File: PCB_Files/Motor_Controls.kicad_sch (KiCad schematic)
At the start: 10 parts, among them U1 TB6612FNG, U3 TB6612FNG

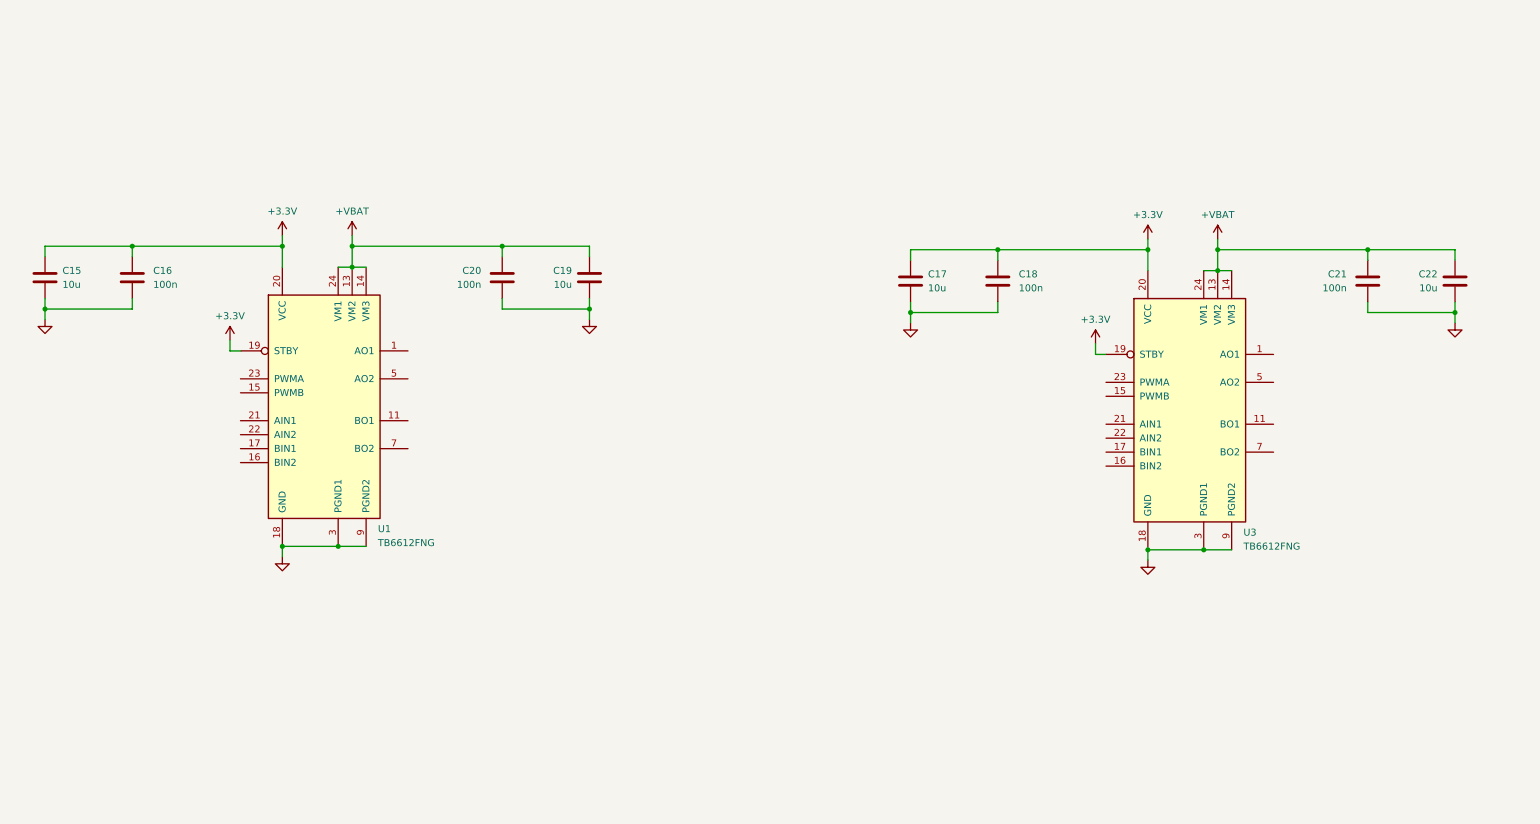
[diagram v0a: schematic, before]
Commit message: Began laying out power schematic and motor controller schematic
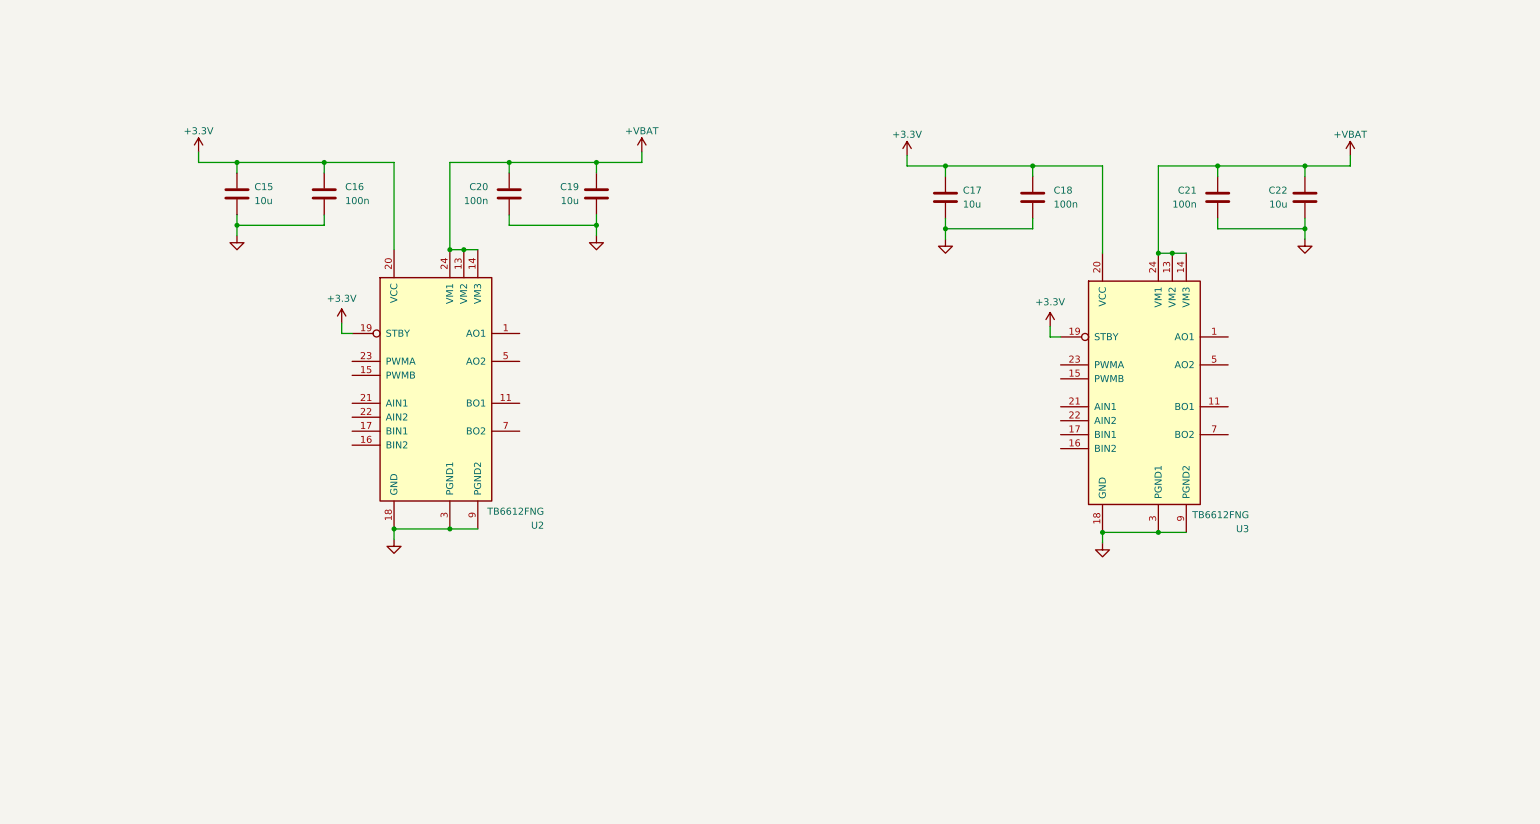
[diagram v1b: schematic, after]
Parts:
- renumbered U1 to U2
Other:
- moved on the sheet: C15, C16, C19, C20, U2

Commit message: Completed motor control schematic sheet and related MCU pin outs.
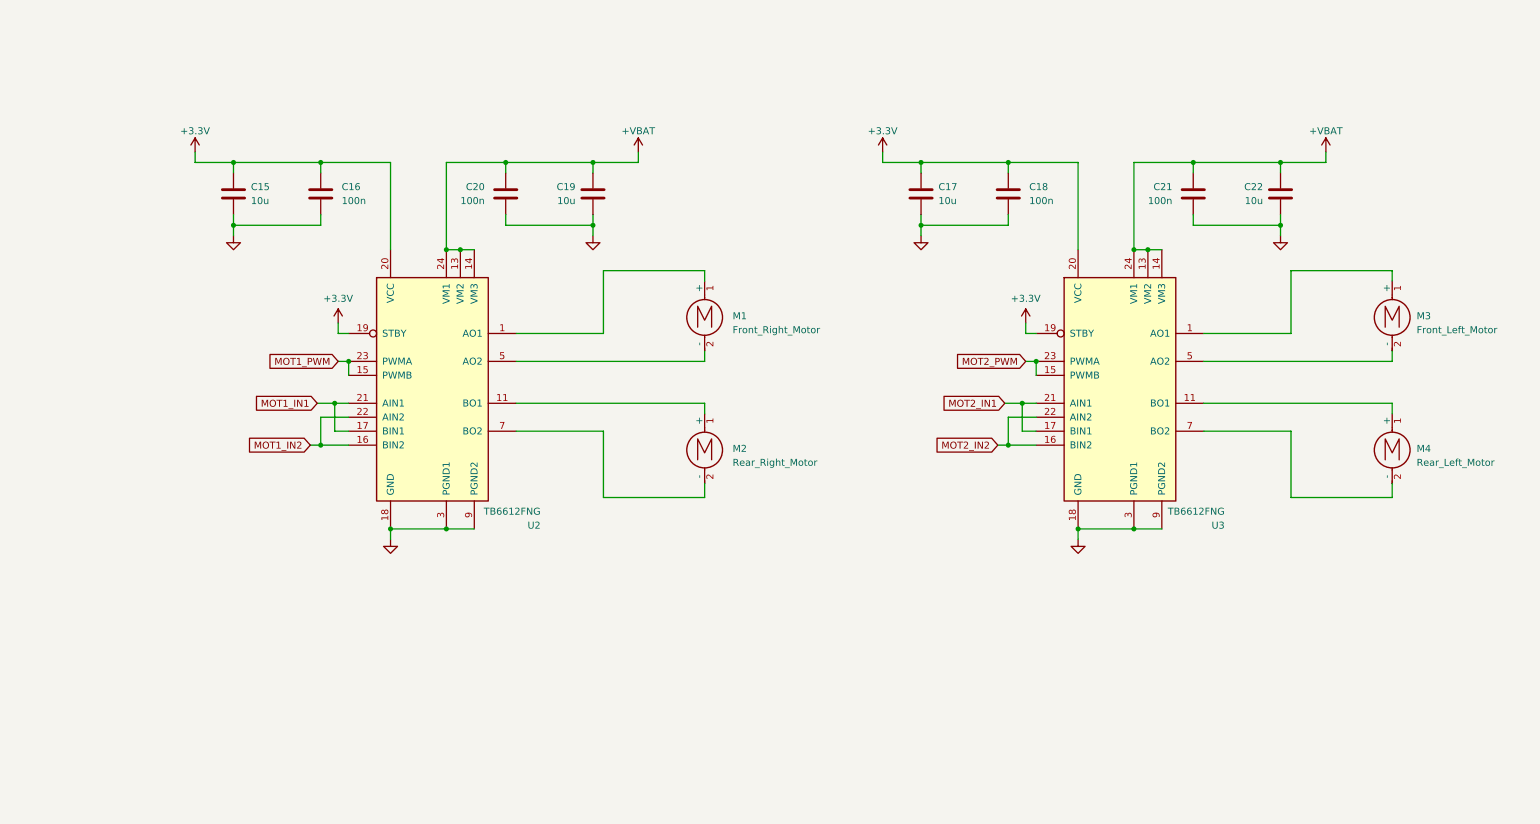
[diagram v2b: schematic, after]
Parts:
- added M1: Front_Right_Motor, symbol Motor:Motor_DC
- added M2: Rear_Right_Motor, symbol Motor:Motor_DC
- added M3: Front_Left_Motor, symbol Motor:Motor_DC
- added M4: Rear_Left_Motor, symbol Motor:Motor_DC
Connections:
- net at U3.1 (AO1), U3.2 (AO1): now also M3.1 (+)
- net at U3.11 (BO1), U3.12 (BO1): now also M4.1 (+)
- net MOT2_PWM: now reaches U3.15 (PWMB)
- net MOT2_PWM: now also U3.23 (PWMA)
- net MOT2_IN2: now reaches U3.16 (BIN2)
- net MOT2_IN2: now also U3.22 (AIN2)
- net MOT2_IN1: now reaches U3.17 (BIN1)
- net MOT2_IN1: now also U3.21 (AIN1)
- net at U3.5 (AO2), U3.6 (AO2): now also M3.2 (-)
- net at U3.7 (BO2), U3.8 (BO2): now also M4.2 (-)
- net at U2.1 (AO1), U2.2 (AO1): now also M1.1 (+)
- net at U2.11 (BO1), U2.12 (BO1): now also M2.1 (+)
- net MOT1_PWM: now reaches U2.15 (PWMB)
- net MOT1_PWM: now also U2.23 (PWMA)
- net MOT1_IN2: now reaches U2.16 (BIN2)
- net MOT1_IN2: now also U2.22 (AIN2)
- net MOT1_IN1: now reaches U2.17 (BIN1)
- net MOT1_IN1: now also U2.21 (AIN1)
- net at U2.5 (AO2), U2.6 (AO2): now also M1.2 (-)
- net at U2.7 (BO2), U2.8 (BO2): now also M2.2 (-)
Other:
- moved on the sheet: C15, C16, C17, C18, C19, C20, C21, C22, U2, U3

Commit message: Cleaned up all ERC errors and warnings due to missing Power Flags or misaligned grid.
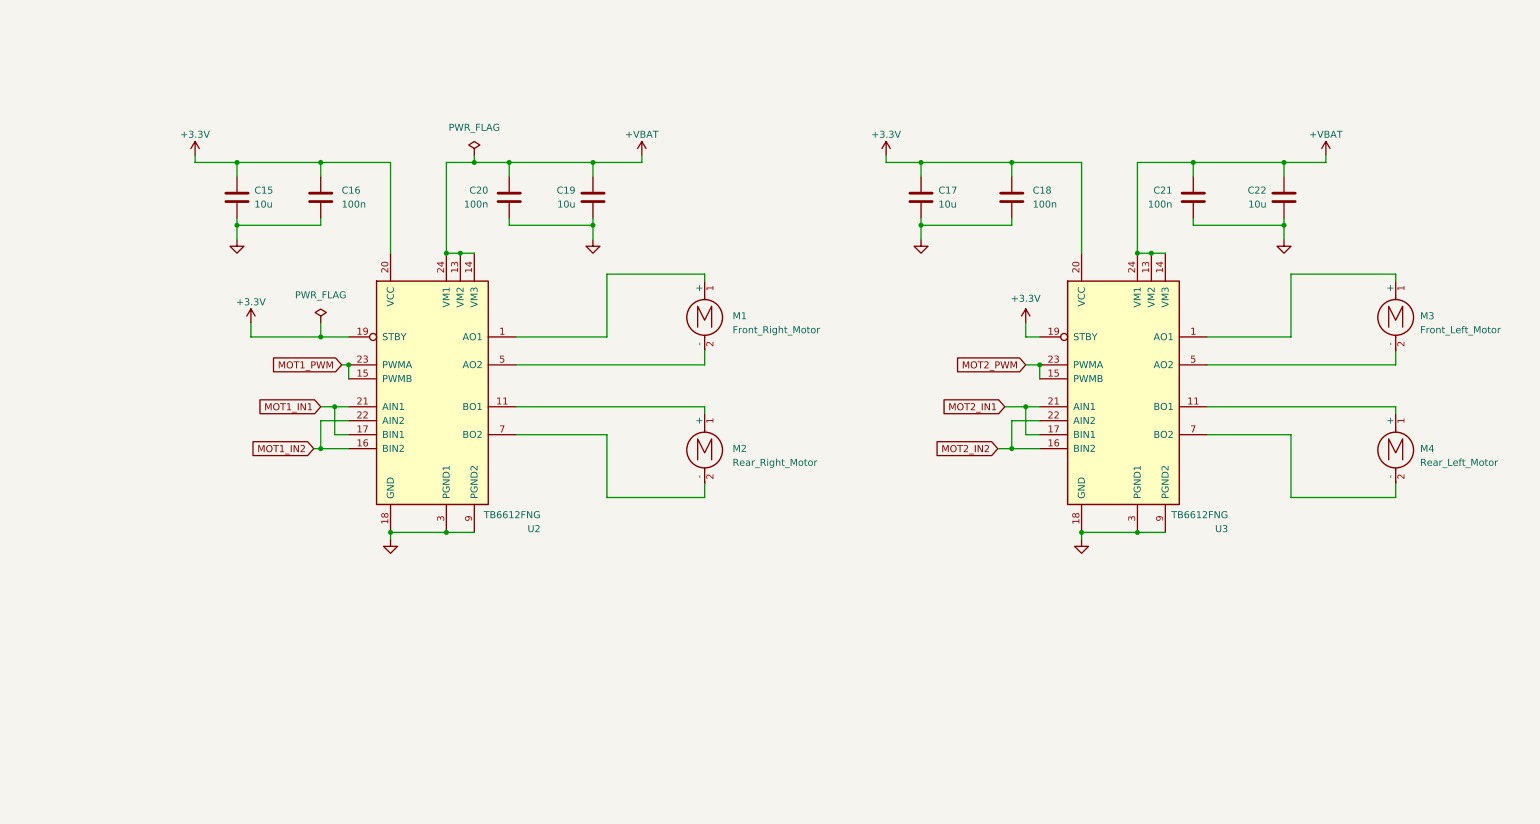
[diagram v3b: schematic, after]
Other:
- moved on the sheet: C15, C16, C17, C18, C19, C20, C21, C22, M3, M4, U2, U3

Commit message: General schematic clean up and footprint allocation.
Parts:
- C15, C16, C17, C18, C19, C20, C21, C22: footprint (none) -> Capacitor_SMD:C_0603_1608Metric
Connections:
- net +3.3V renamed +3V3
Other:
- note added: "MOTOR CONTROLLER - LEFT WHEELS"
- note added: "MOTOR CONTROLLER - RIGHT WHEELS"
- moved on the sheet: C15, C16, C17, C18, C19, C20, C21, C22, M1, M2, M3, M4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

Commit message: Added RadioMaster 2S Battery information to power schematic sheet.
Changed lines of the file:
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@@
-	)
-	(junction
-		(at 179.07 85.09)
-		(diameter 0)
-		(color 0 0 0 0)
 	)
 	(junction
@@
 	(wire
 		(pts
-			(xy 179.07 85.09) (xy 184.15 85.09)
+			(xy 166.37 85.09) (xy 184.15 85.09)
 		)
 		(stroke
@@
 	(wire
 		(pts
-			(xy 179.07 82.55) (xy 179.07 85.09)
-		)
-		(stroke
-			(width 0)
-			(type default)
-		)
-	)
-	(wire
-		(pts
 			(xy 29.21 64.77) (xy 45.72 64.77)
 		)
@@
 		(pts
 			(xy 102.87 52.07) (xy 102.87 53.34)
-		)
-		(stroke
-			(width 0)
-			(type default)
-		)
-	)
-	(wire
-		(pts
-			(xy 166.37 85.09) (xy 179.07 85.09)
 		)
 		(stroke
@@
 					(unit 1)
 				)
-			)
-		)
-	)
-	(symbol
-		(lib_id "power:PWR_FLAG")
-		(at 179.07 82.55 0)
-		(unit 1)
-		(body_style 1)
-		(exclude_from_sim no)
-		(in_bom yes)
-		(on_board yes)
-		(in_pos_files yes)
-		(dnp no)
-		(fields_autoplaced yes)
-		(property "Reference" "#FLG07"
-			(at 179.07 80.645 0)
-			(hide yes)
-			(show_name no)
-			(do_not_autoplace no)
-			(effects
-				(font
-					(size 1.27 1.27)
-				)
-			)
-		)
-		(property "Value" "PWR_FLAG"
-			(at 179.07 77.47 0)
-			(show_name no)
-			(do_not_autoplace no)
-			(effects
-				(font
-					(size 1.27 1.27)
-				)
-			)
-		)
-		(property "Footprint" ""
-			(at 179.07 82.55 0)
-			(hide yes)
-			(show_name no)
-			(do_not_autoplace no)
-			(effects
-				(font
-					(size 1.27 1.27)
-				)
-			)
-		)
-		(property "Datasheet" ""
-			(at 179.07 82.55 0)
-			(hide yes)
-			(show_name no)
-			(do_not_autoplace no)
-			(effects
-				(font
-					(size 1.27 1.27)
-				)
-			)
-		)
-		(property "Description" "Special symbol for telling ERC where power comes from"
-			(at 179.07 82.55 0)
-			(hide yes)
-			(show_name no)
-			(do_not_autoplace no)
-			(effects
-				(font
-					(size 1.27 1.27)
-				)
-			)
-		)
-		(pin "1"
-		)
-		(instances
-			(project "Sensor_Integration_Board"
-				(path "/0eab3e03-be91-4947-b3db-b5c169582a4b/a2ad5281-e4f1-42dc-9117-9489a5cb988a"
-					(reference "#FLG07")
-					(unit 1)
-				)

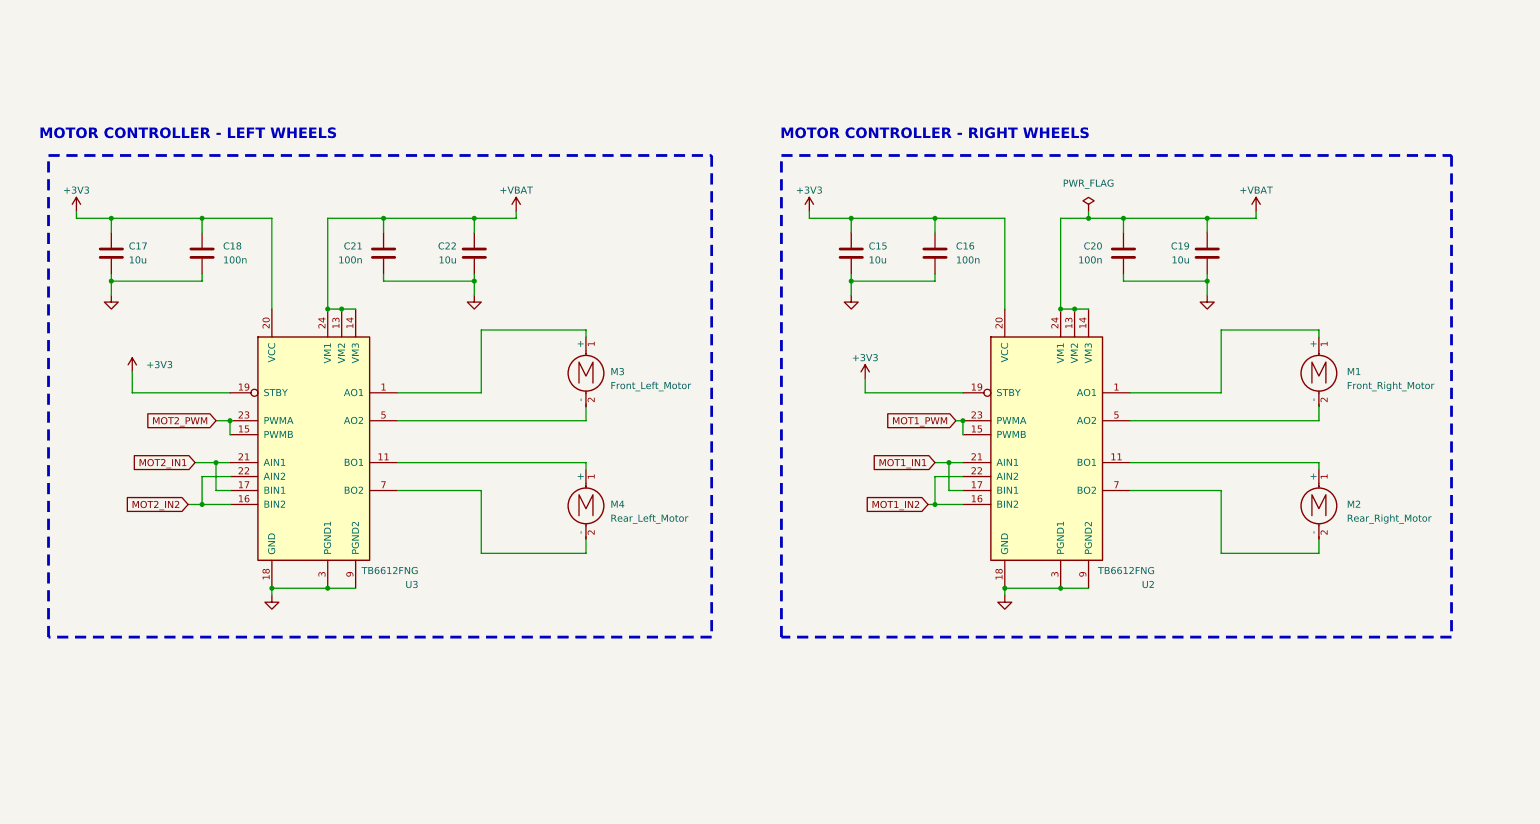
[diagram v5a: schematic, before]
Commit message: Added indicator and debug LED's to various outputs such as buck VOUT, ldo regulator VOUT, motor outputs, and status LED for MCU.
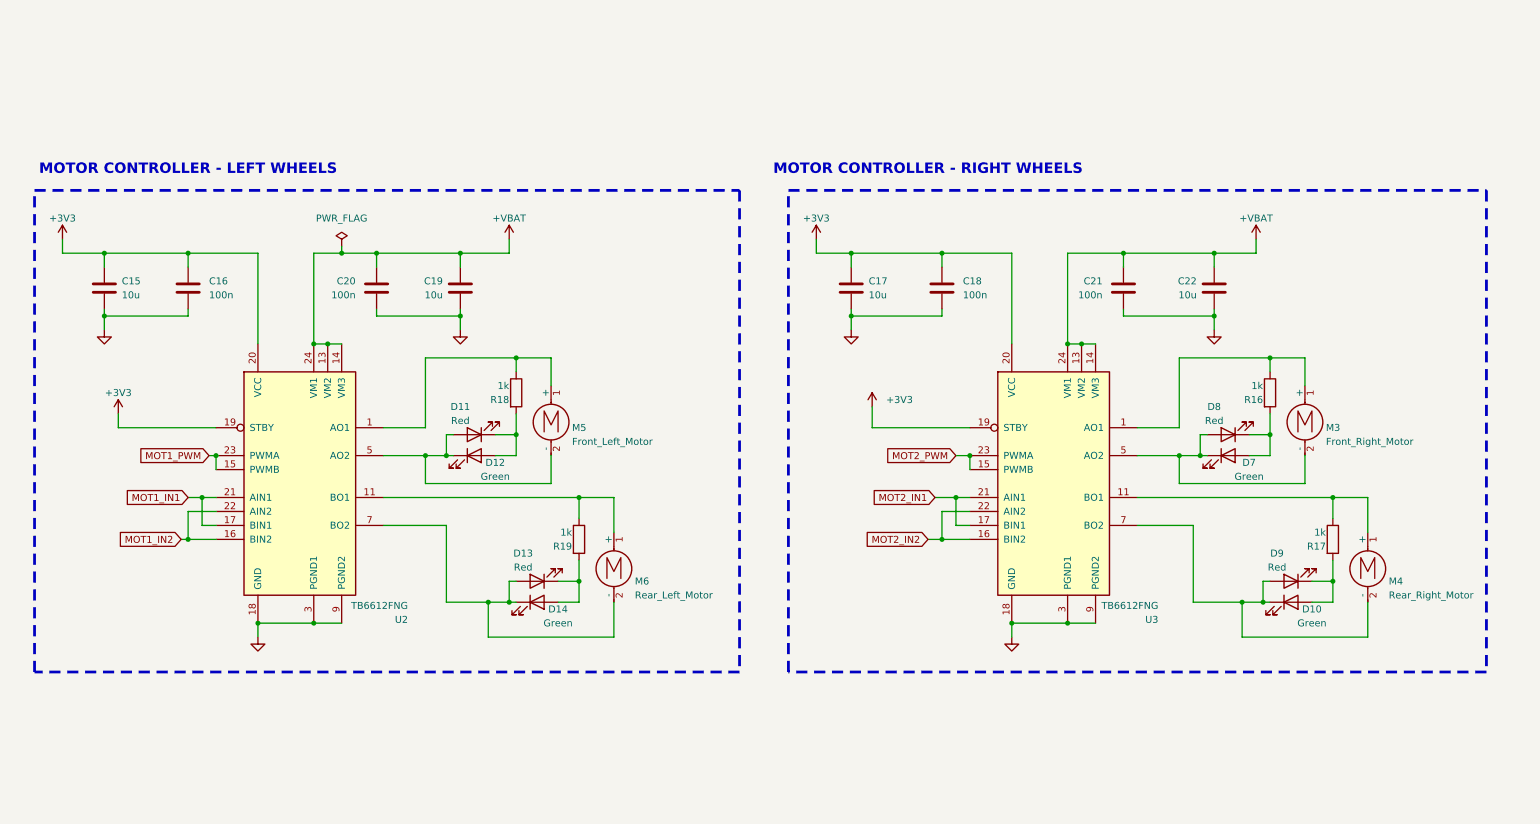
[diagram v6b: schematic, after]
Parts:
- removed M1: Front_Right_Motor, symbol Motor:Motor_DC
- removed M2: Rear_Right_Motor, symbol Motor:Motor_DC
- added D10, D12, D14, D7: Green, symbol Device:LED
- added D11, D13, D8, D9: Red, symbol Device:LED
- added M5: Front_Left_Motor, symbol Motor:Motor_DC
- added M6: Rear_Left_Motor, symbol Motor:Motor_DC
- added R16, R17, R18, R19: 1k, symbol Device:R
- M3: value Front_Left_Motor -> Front_Right_Motor
- M4: value Rear_Left_Motor -> Rear_Right_Motor
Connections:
- net at M4.1 (+), U3.11 (BO1), U3.12 (BO1): now also R17.1
- net at M4.2 (-), U3.7 (BO2), U3.8 (BO2): now also D10.1 (K), D9.2 (A)
- net at M3.1 (+), U3.1 (AO1), U3.2 (AO1): now also R16.1
- net at M3.2 (-), U3.5 (AO2), U3.6 (AO2): now also D7.1 (K), D8.2 (A)
- net at U2.11 (BO1), U2.12 (BO1): now also M6.1 (+), R19.1
- net at U2.7 (BO2), U2.8 (BO2): now also D13.2 (A), D14.1 (K), M6.2 (-)
- net at U2.1 (AO1), U2.2 (AO1): now also M5.1 (+), R18.1
- net at U2.5 (AO2), U2.6 (AO2): now also D11.2 (A), D12.1 (K), M5.2 (-)
- new net: D10.2 (A), D9.1 (K), R17.2
- new net: D13.1 (K), D14.2 (A), R19.2
- new net: D11.1 (K), D12.2 (A), R18.2
- new net: D7.2 (A), D8.1 (K), R16.2
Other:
- moved on the sheet: C15, C16, C17, C18, C19, C20, C21, C22, M3, U2, U3

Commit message: Cleaned up Bi-directional LED indicator schematic layout for motor controllers.
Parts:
- removed D10, D7: Green, symbol Device:LED
- removed D8, D9: Red, symbol Device:LED
- removed M6: Rear_Left_Motor, symbol Motor:Motor_DC
- removed R16, R17: 1k, symbol Device:R
- added D15, D16: Red, symbol Device:LED
- added D17, D18: Green, symbol Device:LED
- added M2: Left_Rear_Motor, symbol Motor:Motor_DC
- added R20, R21: 1k, symbol Device:R
- M1: renamed from M5; value Front_Left_Motor -> Left_Front_Motor
- M3: value Front_Right_Motor -> Right_Front_Motor
- M4: value Rear_Right_Motor -> Right_Rear_Motor
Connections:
- net at M4.1 (+), U3.11 (BO1), U3.12 (BO1): now also R21.1
- net at R19.1, U2.11 (BO1), U2.12 (BO1): now also M2.1 (+)
- net at M3.2 (-), U3.5 (AO2), U3.6 (AO2): now also D15.2 (A), D17.1 (K)
- net at M4.2 (-), U3.7 (BO2), U3.8 (BO2): now also D16.2 (A), D18.1 (K)
- net at M3.1 (+), U3.1 (AO1), U3.2 (AO1): now also R20.1
- net at D13.2 (A), D14.1 (K), U2.7 (BO2)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: now also M2.2 (-)
- new net: D15.1 (K), D17.2 (A), R20.2
- new net: D16.1 (K), D18.2 (A), R21.2
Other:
- moved on the sheet: C19, C20, C21, C22, D11, D12, M1, R18
